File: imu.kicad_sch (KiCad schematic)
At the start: 2 parts, among them U1 LSM6DSL, U2 LIS2MDL

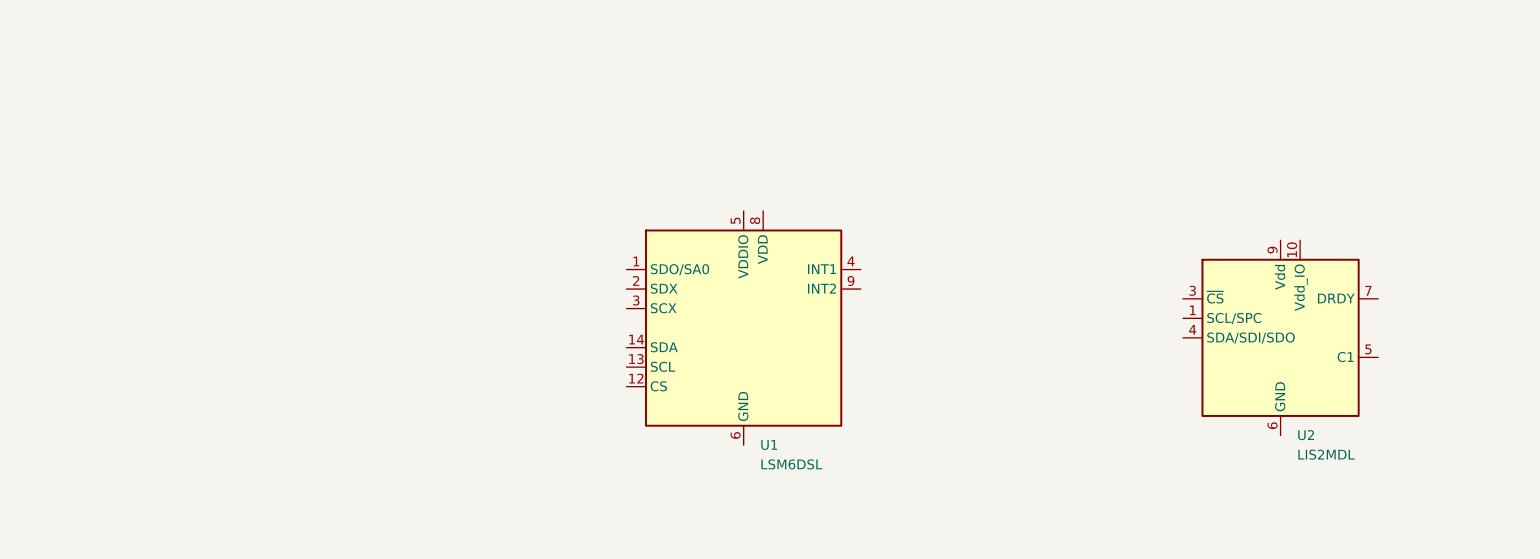
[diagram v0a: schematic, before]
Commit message: Power and IO Schematics for ICs
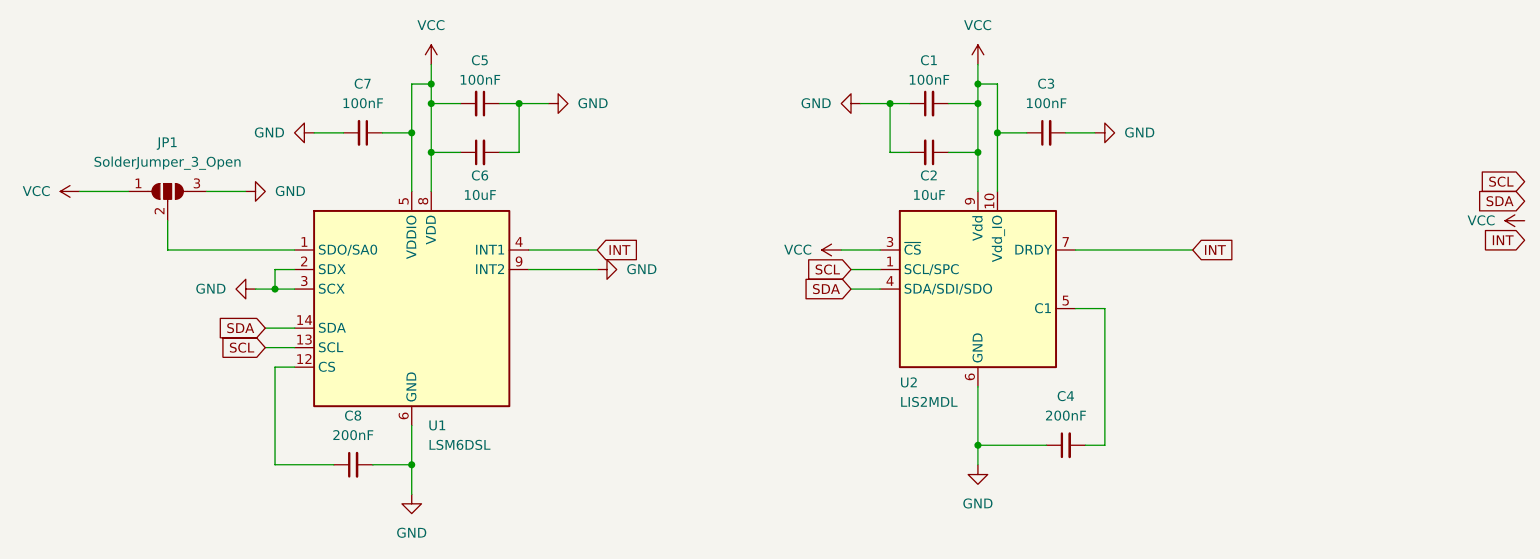
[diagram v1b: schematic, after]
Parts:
- added C1, C3, C5, C7: 100nF, symbol Device:C_Small
- added C2, C6: 10uF, symbol Device:C_Small
- added C4, C8: 200nF, symbol Device:C_Small
- added JP1: SolderJumper_3_Open, Jumper:SolderJumper-3_P1.3mm_Open_RoundedPad1.0x1.5mm, symbol Jumper:SolderJumper_3_Open
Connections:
- net SCL: now reaches U2.1 (SCL/SPC)
- net SCL: now also U1.13 (SCL)
- net VCC: now reaches U2.10 (Vdd_IO)
- net VCC: now also U1.5 (VDDIO), U1.8 (VDD), U2.3 (~{CS}), U2.9 (Vdd), C1.2, C2.1, C3.1, C5.2, C6.1, C7.1, JP1.1 (A)
- net SDA: now reaches U2.4 (SDA/SDI/SDO)
- net SDA: now also U1.14 (SDA)
- net at U2.5 (C1): now also C4.2
- net GND: now reaches U2.6 (GND), U2.8 (GND)
- net GND: now also U1.2 (SDX), U1.3 (SCX), U1.6 (GND), U1.7 (GND), U1.9 (INT2), C1.1, C2.2, C3.2, C4.1, C5.1, C6.2, C7.2, C8.2, JP1.3 (B)
- net INT: now reaches U2.7 (DRDY)
- net INT: now also U1.4 (INT1)
- net at U1.1 (SDO/SA0): now also JP1.2 (C)
- net at U1.12 (CS): now also C8.1
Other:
- moved on the sheet: U1, U2

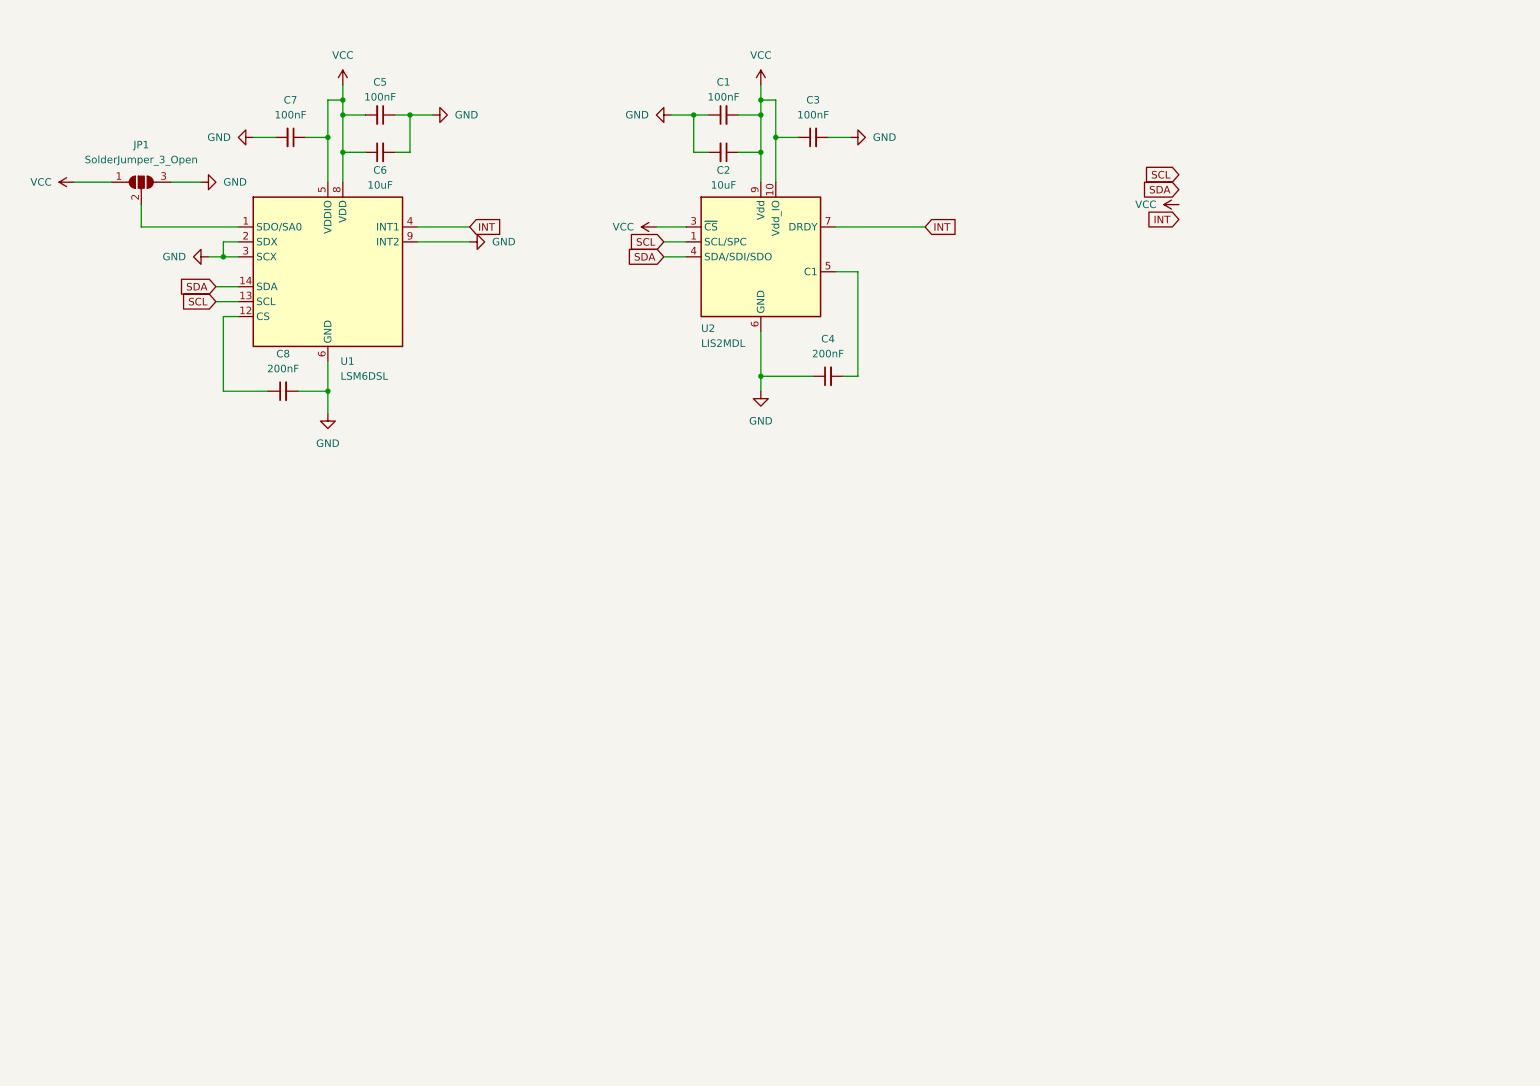
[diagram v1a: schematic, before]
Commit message: Create Schematic for IMU-Breakout Board
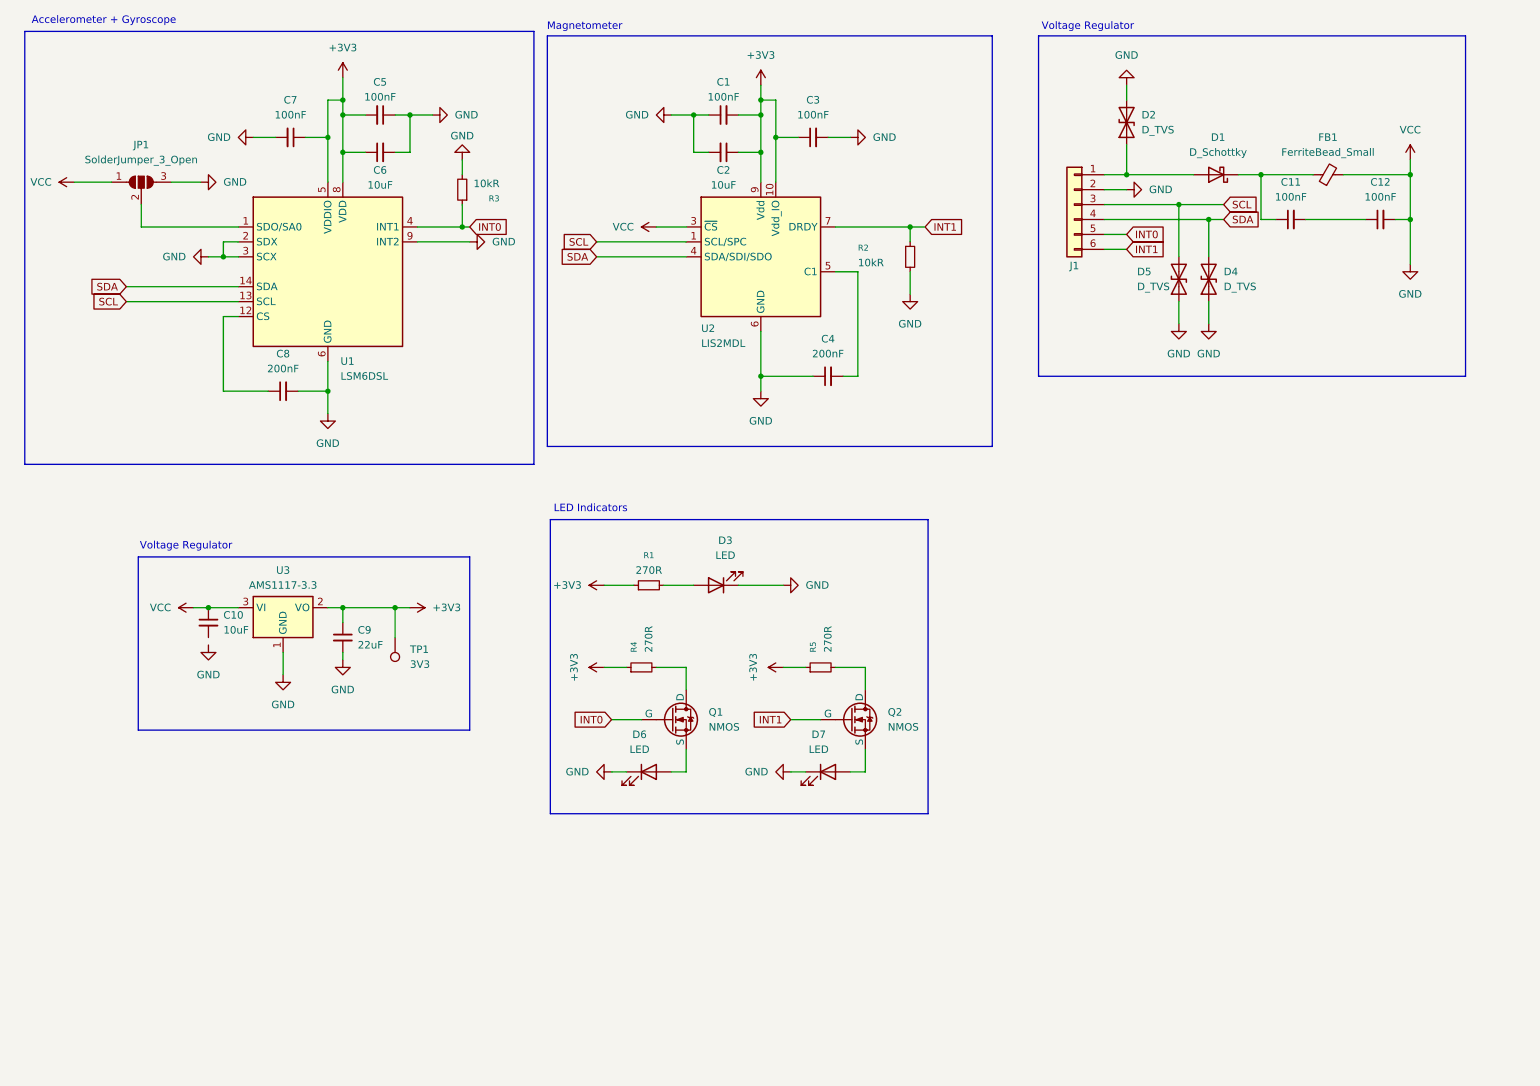
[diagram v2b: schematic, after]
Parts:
- added C10: 10uF, symbol Device:C_Small
- added C11, C12: 100nF, symbol Device:C_Small
- added C9: 22uF, symbol Device:C_Small
- added D1: D_Schottky, symbol Device:D_Schottky
- added D2, D4, D5: D_TVS, symbol Device:D_TVS
- added D3, D6, D7: LED, symbol Device:LED
- added FB1: FerriteBead_Small, symbol Device:FerriteBead_Small
- added J1: Conn_01x06, symbol Connector_Generic:Conn_01x06
- added Q1, Q2: NMOS, symbol Simulation_SPICE:NMOS
- added R1, R4, R5: 270R, symbol Device:R_Small
- added R2, R3: 10kR, symbol Device:R_Small
- added TP1: 3V3, symbol Connector:TestPoint
- added U3: AMS1117-3.3, Package_TO_SOT_SMD:SOT-223-3_TabPin2, symbol Regulator_Linear:AMS1117-3.3
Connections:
- net GND: now also JP1.1 (A), U2.3 (~{CS}), C10.1, C12.2, C9.2, D2.2 (A2), D3.1 (K), D4.1 (A1), D5.1 (A1), D6.1 (K), D7.1 (K), FB1.2, J1.2 (Pin_2), R2.2, R3.2, U3.1 (GND), U3.3 (VI)
- net SCL: now also D5.2 (A2), J1.3 (Pin_3)
- net SDA: now also D4.2 (A2), J1.4 (Pin_4)
- net INT renamed INT0
- net INT0: now also J1.5 (Pin_5), Q1.2 (G), R3.1; no longer U2.7 (DRDY)
- net VCC renamed +3V3
- net +3V3: now also C9.1, R1.1, R4.1, R5.1, TP1.1, U3.2 (VO); no longer JP1.1 (A), U2.3 (~{CS})
- new net: Q2.1 (D), R5.2
- new net: Q1.1 (D), R4.2
- new net: D6.2 (A), Q1.3 (S)
- new net: D7.2 (A), Q2.3 (S)
- new net: D1.2 (A), D2.1 (A1), J1.1 (Pin_1)
- new net: C11.2, C12.1
- new net: C11.1, D1.1 (K), FB1.1
- new net: D3.2 (A), R1.2
- new net INT1: J1.6 (Pin_6), Q2.2 (G), R2.1, U2.7 (DRDY)
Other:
- note added: "Accelerometer + Gyroscope"
- note added: "LED Indicators"
- note added: "Magnetometer"
- note added: "Voltage Regulator"

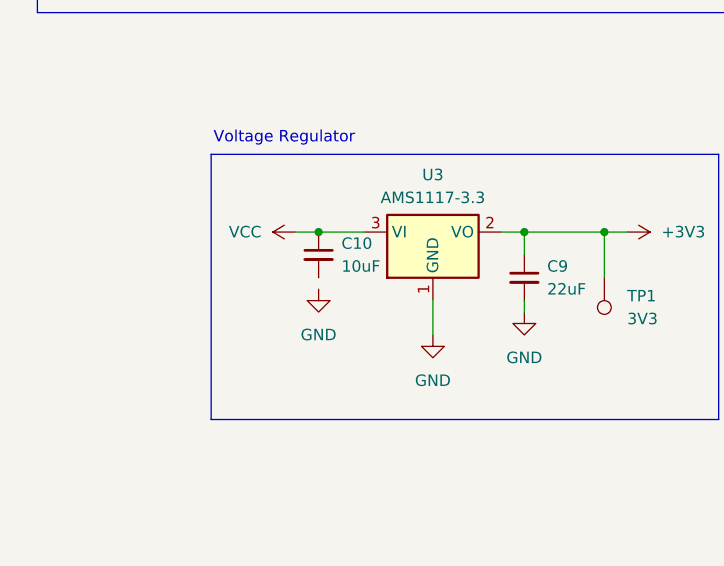
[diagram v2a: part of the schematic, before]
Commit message: Add Footprint Names
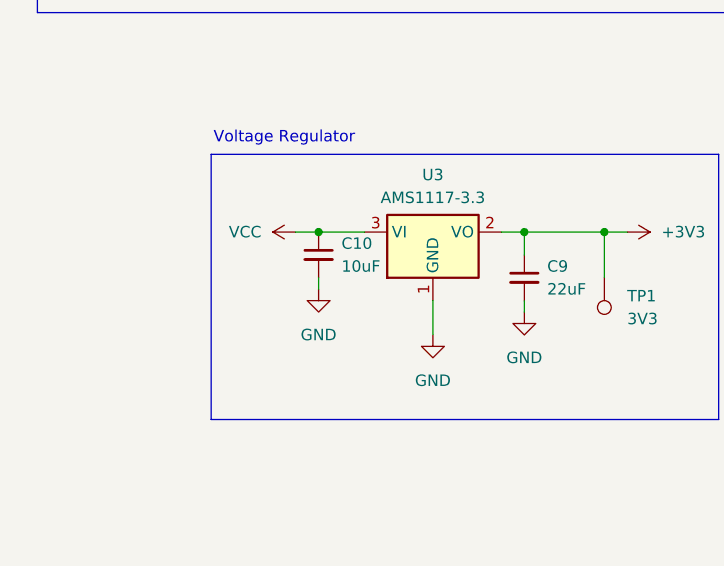
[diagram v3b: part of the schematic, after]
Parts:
- C1, C10, C11, C12, C2, C3, C4, C5, C6, C7, C8, C9: footprint (none) -> Capacitor_SMD:C_0805_2012Metric_Pad1.18x1.45mm_HandSolder
- D1: footprint (none) -> Diode_SMD:D_SOD-123F
- D2: footprint (none) -> Diode_SMD:D_SMB-SMC_Universal_Handsoldering
- D3, D6, D7: footprint (none) -> LED_SMD:LED_0805_2012Metric_Pad1.15x1.40mm_HandSolder
- D4, D5: footprint (none) -> Diode_SMD:D_SOD-323_HandSoldering
- FB1: footprint (none) -> Inductor_SMD:L_0805_2012Metric_Pad1.05x1.20mm_HandSolder
- J1: footprint (none) -> Connector_JST:JST_XH_B6B-XH-A_1x06_P2.50mm_Vertical
- R1, R2, R3, R4, R5: footprint (none) -> Resistor_SMD:R_0805_2012Metric_Pad1.20x1.40mm_HandSolder
- TP1: footprint (none) -> TestPoint:TestPoint_Pad_1.5x1.5mm
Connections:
- net GND: now also C10.2
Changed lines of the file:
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@@
 	(wire
 		(pts
+			(xy 53.34 120.65) (xy 53.34 121.92)
+		)
+		(stroke
+			(width 0)
+			(type default)
+		)
+	)
+	(wire
+		(pts
 			(xy 68.58 78.74) (xy 73.66 78.74)
 		)
@@
 			)
 		)
-		(property "Footprint" ""
+		(property "Footprint" "Diode_SMD:D_SOD-323_HandSoldering"
 			(at 223.52 59.69 0)
 			(effects
@@
 			)
 		)
-		(property "Footprint" ""
+		(property "Footprint" "Resistor_SMD:R_0805_2012Metric_Pad1.20x1.40mm_HandSolder"
 			(at 157.48 125.73 0)
 			(effects
@@
 			)
 		)
-		(property "Footprint" ""
+		(property "Footprint" "LED_SMD:LED_0805_2012Metric_Pad1.15x1.40mm_HandSolder"
 			(at 158.75 143.51 0)
 			(effects
@@
 			)
 		)
-		(property "Footprint" ""
+		(property "Footprint" "Resistor_SMD:R_0805_2012Metric_Pad1.20x1.40mm_HandSolder"
 			(at 172.72 55.88 0)
 			(effects
@@
 			)
 		)
-		(property "Footprint" ""
+		(property "Footprint" "Capacitor_SMD:C_0805_2012Metric_Pad1.18x1.45mm_HandSolder"
 			(at 82.55 38.1 0)
 			(effects
@@
 			)
 		)
-		(property "Footprint" ""
+		(property "Footprint" "Capacitor_SMD:C_0805_2012Metric_Pad1.18x1.45mm_HandSolder"
 			(at 156.21 35.56 0)
 			(effects
@@
 			)
 		)
-		(property "Footprint" ""
+		(property "Footprint" "Capacitor_SMD:C_0805_2012Metric_Pad1.18x1.45mm_HandSolder"
 			(at 53.34 118.11 0)
 			(effects
@@
 			)
 		)
-		(property "Footprint" ""
+		(property "Footprint" "LED_SMD:LED_0805_2012Metric_Pad1.15x1.40mm_HandSolder"
 			(at 128.27 143.51 0)
 			(effects
@@
 			)
 		)
-		(property "Footprint" ""
+		(property "Footprint" "Connector_JST:JST_XH_B6B-XH-A_1x06_P2.50mm_Vertical"
 			(at 200.66 46.99 0)
 			(effects
@@
 			)
 		)
-		(property "Footprint" ""
+		(property "Footprint" "Resistor_SMD:R_0805_2012Metric_Pad1.20x1.40mm_HandSolder"
 			(at 96.52 44.45 0)
 			(effects
@@
 			)
 		)
-		(property "Footprint" ""
+		(property "Footprint" "Capacitor_SMD:C_0805_2012Metric_Pad1.18x1.45mm_HandSolder"
 			(at 140.97 38.1 0)
 			(effects
@@
 			)
 		)
-		(property "Footprint" ""
+		(property "Footprint" "Capacitor_SMD:C_0805_2012Metric_Pad1.18x1.45mm_HandSolder"
 			(at 67.31 35.56 0)
 			(effects
@@
 			)
 		)
-		(property "Footprint" ""
+		(property "Footprint" "Diode_SMD:D_SMB-SMC_Universal_Handsoldering"
 			(at 209.55 33.02 0)
 			(effects
@@
 			)
 		)
-		(property "Footprint" ""
+		(property "Footprint" "Capacitor_SMD:C_0805_2012Metric_Pad1.18x1.45mm_HandSolder"
 			(at 252.73 49.53 0)
 			(effects
@@
 			)
 		)
-		(property "Footprint" ""
+		(property "Footprint" "Capacitor_SMD:C_0805_2012Metric_Pad1.18x1.45mm_HandSolder"
 			(at 158.75 76.2 0)
 			(effects
@@
 			)
 		)
-		(property "Footprint" ""
+		(property "Footprint" "Capacitor_SMD:C_0805_2012Metric_Pad1.18x1.45mm_HandSolder"
 			(at 66.04 78.74 0)
 			(effects
@@
 			)
 		)
-		(property "Footprint" ""
+		(property "Footprint" "Resistor_SMD:R_0805_2012Metric_Pad1.20x1.40mm_HandSolder"
 			(at 127 125.73 0)
 			(effects
@@
 			)
 		)
-		(property "Footprint" ""
+		(property "Footprint" "Capacitor_SMD:C_0805_2012Metric_Pad1.18x1.45mm_HandSolder"
 			(at 140.97 31.75 0)
 			(effects
@@
 			)
 		)
-		(property "Footprint" ""
+		(property "Footprint" "Diode_SMD:D_SOD-323_HandSoldering"
 			(at 218.44 59.69 0)
 			(effects
@@
 			)
 		)
-		(property "Footprint" ""
+		(property "Footprint" "Inductor_SMD:L_0805_2012Metric_Pad1.05x1.20mm_HandSolder"
 			(at 243.84 43.688 90)
 			(effects
@@
 			)
 		)
-		(property "Footprint" ""
+		(property "Footprint" "Diode_SMD:D_SOD-123F"
 			(at 224.79 41.91 0)
 			(effects
@@
 			)
 		)
-		(property "Footprint" ""
+		(property "Footprint" "Capacitor_SMD:C_0805_2012Metric_Pad1.18x1.45mm_HandSolder"
 			(at 82.55 31.75 0)
 			(effects
@@
 			)
 		)
-		(property "Footprint" ""
+		(property "Footprint" "Resistor_SMD:R_0805_2012Metric_Pad1.20x1.40mm_HandSolder"
 			(at 128.27 111.76 0)
 			(effects
@@
 			)
 		)
-		(property "Footprint" ""
+		(property "Footprint" "TestPoint:TestPoint_Pad_1.5x1.5mm"
 			(at 80.01 120.65 0)
 			(effects
@@
 			)
 		)
-		(property "Footprint" ""
+		(property "Footprint" "Capacitor_SMD:C_0805_2012Metric_Pad1.18x1.45mm_HandSolder"
 			(at 76.2 120.65 0)
 			(effects
@@
 			)
 		)
-		(property "Footprint" ""
+		(property "Footprint" "LED_SMD:LED_0805_2012Metric_Pad1.15x1.40mm_HandSolder"
 			(at 139.7 111.76 0)
 			(effects
@@
 			)
 		)
-		(property "Footprint" ""
+		(property "Footprint" "Capacitor_SMD:C_0805_2012Metric_Pad1.18x1.45mm_HandSolder"
 			(at 237.49 49.53 0)
 			(effects

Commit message: PCB Design Finished
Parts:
- removed C1, C7: 100nF, Capacitor_SMD:C_0805_2012Metric_Pad1.18x1.45mm_HandSolder, symbol Device:C_Small
- removed C2, C6: 10uF, Capacitor_SMD:C_0805_2012Metric_Pad1.18x1.45mm_HandSolder, symbol Device:C_Small
- removed D6, D7: LED, LED_SMD:LED_0805_2012Metric_Pad1.15x1.40mm_HandSolder, symbol Device:LED
- removed JP1: SolderJumper_3_Open, Jumper:SolderJumper-3_P1.3mm_Open_RoundedPad1.0x1.5mm, symbol Jumper:SolderJumper_3_Open
- removed Q1, Q2: NMOS, symbol Simulation_SPICE:NMOS
- removed R4, R5: 270R, Resistor_SMD:R_0805_2012Metric_Pad1.20x1.40mm_HandSolder, symbol Device:R_Small
- removed TP1: 3V3, TestPoint:TestPoint_Pad_1.5x1.5mm, symbol Connector:TestPoint
- D2: footprint Diode_SMD:D_SMB-SMC_Universal_Handsoldering -> Diode_SMD:D_SMB
- J1: footprint Connector_JST:JST_XH_B6B-XH-A_1x06_P2.50mm_Vertical -> Connector_PinHeader_2.54mm:PinHeader_1x06_P2.54mm_Vertical
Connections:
- net +3V3: now also U2.3 (~{CS})
- net GND: now also C11.2, C12.1, U1.1 (SDO/SA0); no longer C10.1, C12.2, FB1.2, U2.3 (~{CS}), U3.3 (VI)
- net SCL: now also D4.2 (A2), J1.4 (Pin_4); no longer D5.2 (A2), J1.3 (Pin_3)
- net SDA: now also D5.2 (A2), J1.3 (Pin_3); no longer D4.2 (A2), J1.4 (Pin_4)
- new net VCC: C10.1, C12.2, FB1.2, U3.3 (VI)
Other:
- note added: "Power LED"
- note removed: "LED Indicators"
- moved on the sheet: C11, C12
